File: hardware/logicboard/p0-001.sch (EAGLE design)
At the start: 23 parts, among them IC1 74LS07N, IC2 LTC485N, IC3 LTC485N

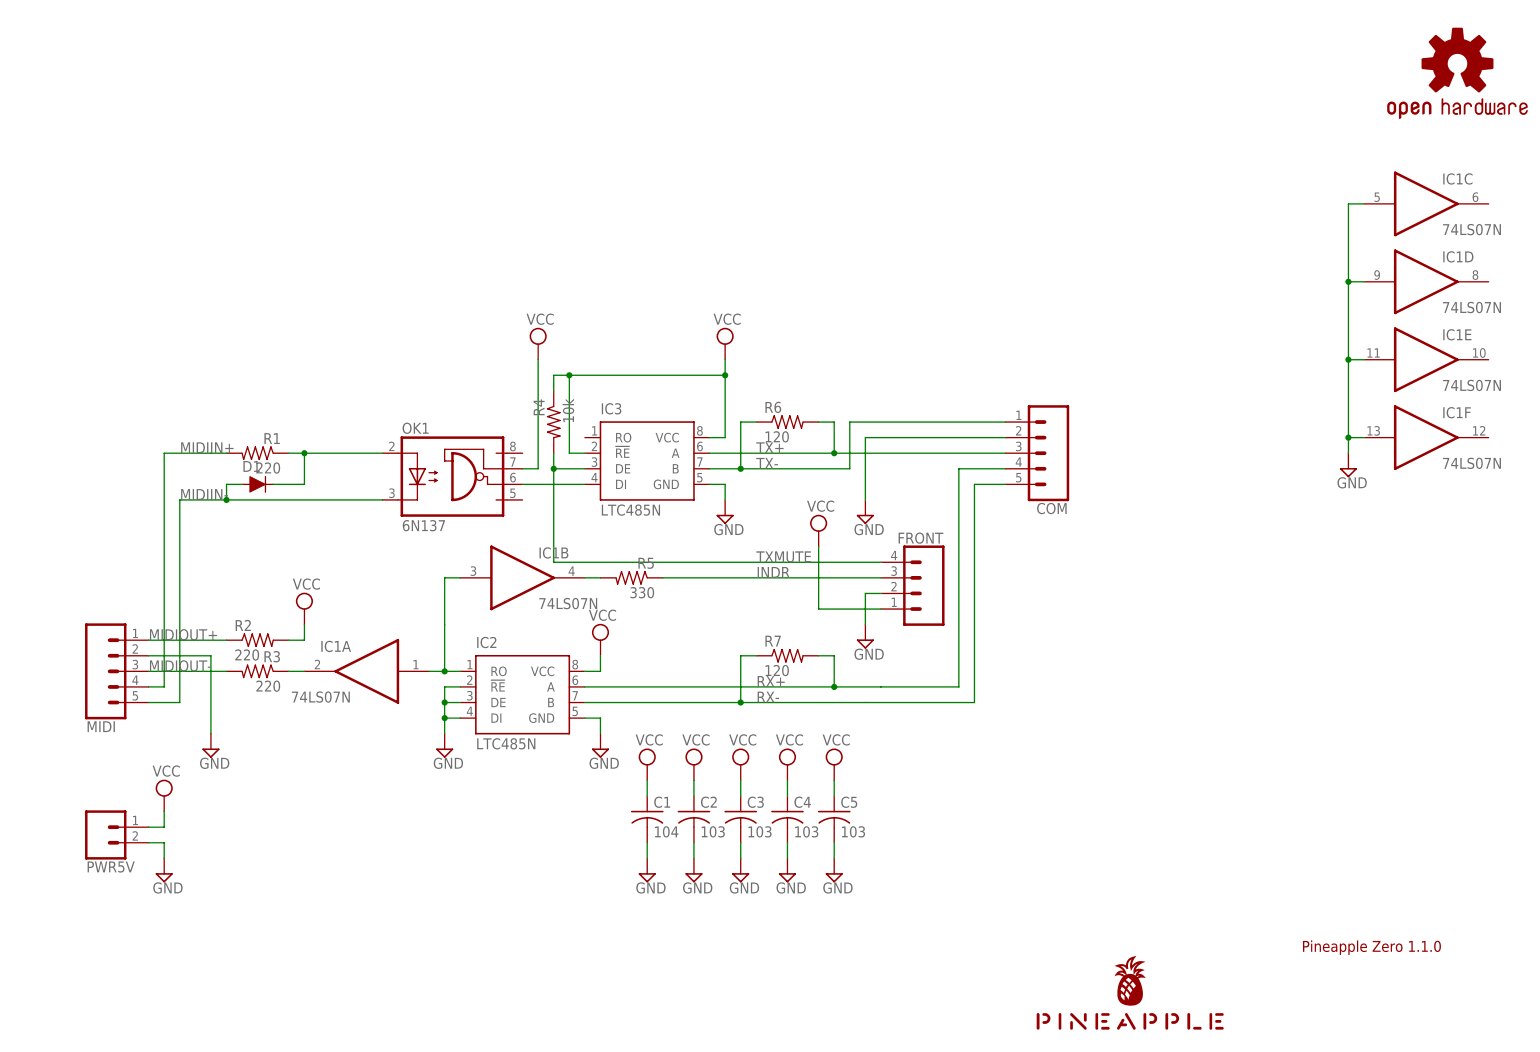
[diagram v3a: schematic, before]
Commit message: Clean up of the schematic.
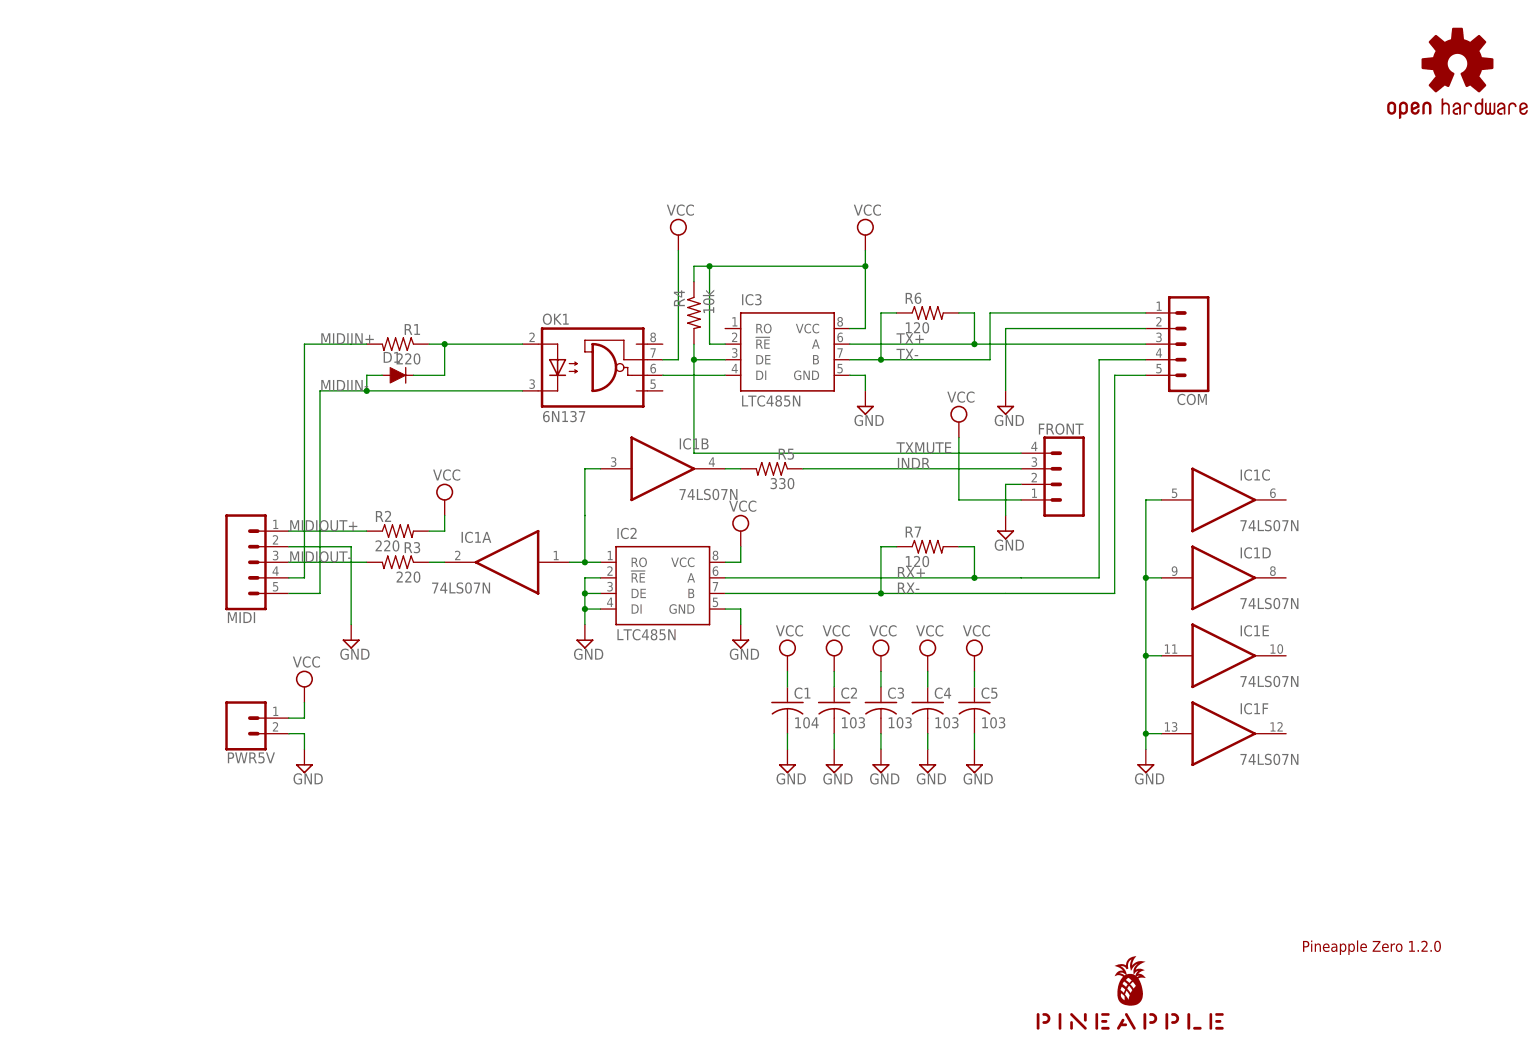
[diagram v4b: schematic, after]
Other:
- note added: "Pineapple Zero 1.2.0"
- note removed: "Pineapple Zero 1.1.0"
- moved on the sheet: C1, C2, C3, C4, C5, COM, D1, FRONT, IC1A, IC1B, IC1C, IC1D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

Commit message: First try.
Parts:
- removed COM, MIDI: (no value), SparkFun-Connectors:CONN_05JST
- removed FRONT: (no value), SparkFun-Connectors:CONN_04JST-PTH
- removed PWR5V: (no value), SparkFun-Connectors:CONN_02JST-PTH-2
- removed R1, R2, R3: 220, resistor:R-US_0204/5
- removed R4: 10k, resistor:R-US_0204/5
- removed R5: 330, resistor:R-US_0204/5
- removed R6, R7: 120, resistor:R-US_0204/5
- added J0: (no value), con-jack:JACK-PLUG0
- added J1, J2, J3: DIN5, SparkFun-Connectors:DIN5
- added LED1, LED2, LED3: (no value), led:LED3MM
- added RN1: (no value), resistor-dil:8R-N
- added RN2: (no value), resistor-net:RN04
- added X1, X2: GLX-S-88M, con-kycon:GLX-S-88M
- C1: value 104 -> (none); device rcl:C-US025-025X050 -> rcl:C-EU025-024X044
- C2, C3, C4, C5: value 103 -> (none); device rcl:C-US025-025X050 -> rcl:C-EU025-024X044
- IC1: value 74LS07N -> 74ALS05N; device 74xx-us:74LS07N -> 74xx-us:74ALS05N
- OK1: value 6N137 -> HCPL2630; device optocoupler:6N137 -> optocoupler:HCPL2630
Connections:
- removed net IND: IC1B.O, R5.2
- removed net INDR: FRONT.3, R5.1
- removed net MIDIIN: IC3.DI, OK1.VO
- removed net MIDIIN+: MIDI.4, R1.2
- removed net MIDIOUT+: MIDI.1, R2.1
- removed net MIDIOUT-: MIDI.3, R3.2
- removed net MIDIOUT-RAW: IC1A.O, R3.1
- removed net TXMUTE: FRONT.4, IC3.DE, R4.2
- new net N$1: J1.4, RN1A.1
- new net N$10: IC1E.O, RN1E.2
- new net N$11: IC1D.O, IC1E.I, RN2.3
- new net N$12: LED1.A, RN1F.2
- new net N$13: LED2.A, RN1G.1
- new net N$14: LED3.A, RN1H.1
- new net N$15: IC1F.O, LED3.C
- new net N$2: IC1C.O, LED2.C
- new net N$3: IC1A.I, IC1C.I, IC3.DI, OK1A.VO1
- new net N$4: J3.5, RN1C.1
- new net N$5: IC1A.O, IC1B.I, RN2.2
- new net N$6: IC1B.O, RN1C.2
- new net N$7: J3.4, RN1B.1
- new net N$8: J2.4, RN1D.1
- new net N$9: J2.5, RN1E.1
- net GND: now also J0.1, J0.2, J2.2, J3.2, LED1.C, OK1A.GND, OK1B.A2, OK1B.C2, X1.S1, X1.S2, X2.S1, X2.S2; no longer COM.2, FRONT.2, IC1C.I, IC1D.I, IC1E.I, IC1F.I, MIDI.2, PWR5V.2
- net MIDIIN-: now also J1.5, OK1A.C1; no longer MIDI.5, OK1.C
- net MIDIINA: now also OK1A.A1, RN1A.2; no longer OK1.A, R1.1
- net MIDIOUT: now also IC1D.I, IC1F.I; no longer IC1A.I, IC1B.I
- net RX+: now also X2.1; no longer COM.4, R7.2
- net RX-: now also X2.2; no longer COM.5, R7.1
- net TX+: now also X1.1; no longer COM.3, R6.2
- net TX-: now also X1.2; no longer COM.1, R6.1
- net VCC: now also IC3.DE, J0.3, OK1A.VCC, RN1B.2, RN1D.2, RN1F.1, RN1G.2, RN1H.2, RN2.1; no longer FRONT.1, OK1.VE, PWR5V.1, R2.2, R4.1
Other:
- moved on the sheet: C1, C2, C3, C4, C5, D1, IC2, IC3

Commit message: Now use Neltron's RJ-45 Jack.
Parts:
- X1, X2: value GLX-S-88M -> NELTRON-7810-XPXC; device con-kycon:GLX-S-88M -> con-rj45:NELTRON-7810-XPXC

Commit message: Rearranged connectors.
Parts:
- added R1: (no value), rcl:R-EU_0204/5
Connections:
- net RX+: now also R1.1
- net RX-: now also R1.2
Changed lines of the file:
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@@
 <part name="SUPPLY30" library="supply2" library_urn="urn:adsk.eagle:library:372" deviceset="VCC" device=""/>
 <part name="LED3" library="led" library_urn="urn:adsk.eagle:library:259" deviceset="LED" device="3MM" package3d_urn="urn:adsk.eagle:package:15797/1"/>
+<part name="R1" library="rcl" library_urn="urn:adsk.eagle:library:334" deviceset="R-EU_" device="0204/5" package3d_urn="urn:adsk.eagle:package:23488/1"/>
 <part name="X1" library="con-rj45" deviceset="NELTRON-7810-XPXC" device=""/>
 <part name="X2" library="con-rj45" deviceset="NELTRON-7810-XPXC" device=""/>
@@
 <attribute name="VALUE" x="142.748" y="73.025" size="1.778" layer="96"/>
 </instance>
+<instance part="R1" gate="G$1" x="160.02" y="66.04" smashed="yes">
+<attribute name="NAME" x="156.21" y="67.5386" size="1.778" layer="95"/>
+<attribute name="VALUE" x="156.21" y="62.738" size="1.778" layer="96"/>
+</instance>
 <instance part="X1" gate="G$1" x="175.26" y="119.38" smashed="yes">
 <attribute name="NAME" x="179.07" y="130.048" size="1.778" layer="95"/>
@@
 <segment>
 <pinref part="IC2" gate="G$1" pin="A"/>
-<wire x1="142.24" y1="60.96" x2="172.72" y2="60.96" width="0.1524" layer="91"/>
+<wire x1="142.24" y1="60.96" x2="152.4" y2="60.96" width="0.1524" layer="91"/>
 <label x="144.78" y="60.96" size="1.778" layer="95"/>
+<pinref part="R1" gate="G$1" pin="1"/>
+<wire x1="152.4" y1="60.96" x2="172.72" y2="60.96" width="0.1524" layer="91"/>
+<wire x1="154.94" y1="66.04" x2="152.4" y2="66.04" width="0.1524" layer="91"/>
+<wire x1="152.4" y1="66.04" x2="152.4" y2="60.96" width="0.1524" layer="91"/>
+<junction x="152.4" y="60.96"/>
 <pinref part="X2" gate="G$1" pin="1"/>
 </segment>
@@
 <segment>
 <pinref part="IC2" gate="G$1" pin="B"/>
-<wire x1="172.72" y1="58.42" x2="142.24" y2="58.42" width="0.1524" layer="91"/>
+<wire x1="172.72" y1="58.42" x2="167.64" y2="58.42" width="0.1524" layer="91"/>
 <label x="144.78" y="58.42" size="1.778" layer="95"/>
+<pinref part="R1" gate="G$1" pin="2"/>
+<wire x1="167.64" y1="58.42" x2="142.24" y2="58.42" width="0.1524" layer="91"/>
+<wire x1="165.1" y1="66.04" x2="167.64" y2="66.04" width="0.1524" layer="91"/>
+<wire x1="167.64" y1="66.04" x2="167.64" y2="58.42" width="0.1524" layer="91"/>
+<junction x="167.64" y="58.42"/>
 <pinref part="X2" gate="G$1" pin="2"/>
 </segment>
